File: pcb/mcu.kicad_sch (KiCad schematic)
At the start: 23 parts, among them J1 AVR-ISP-6, U15 TL431DBZ, U6 ATmega328P-AU, Y1 14.7456 MHz

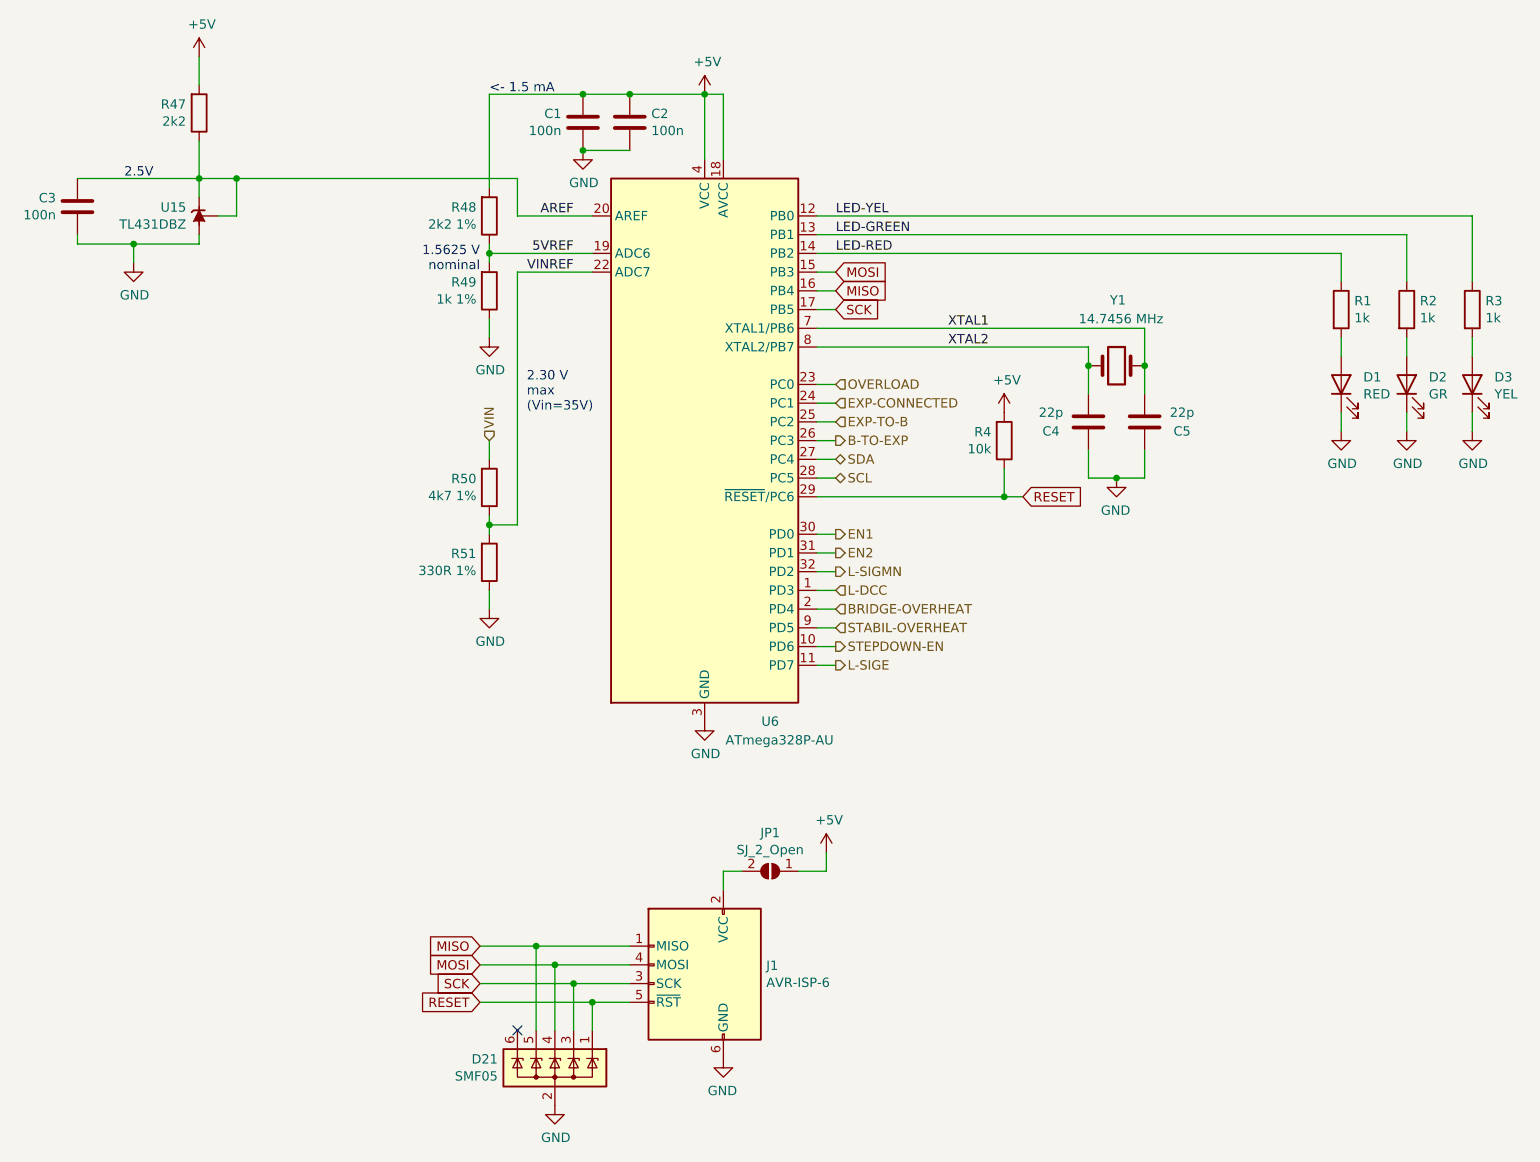
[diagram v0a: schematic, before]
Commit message: Update to KiCad 8.
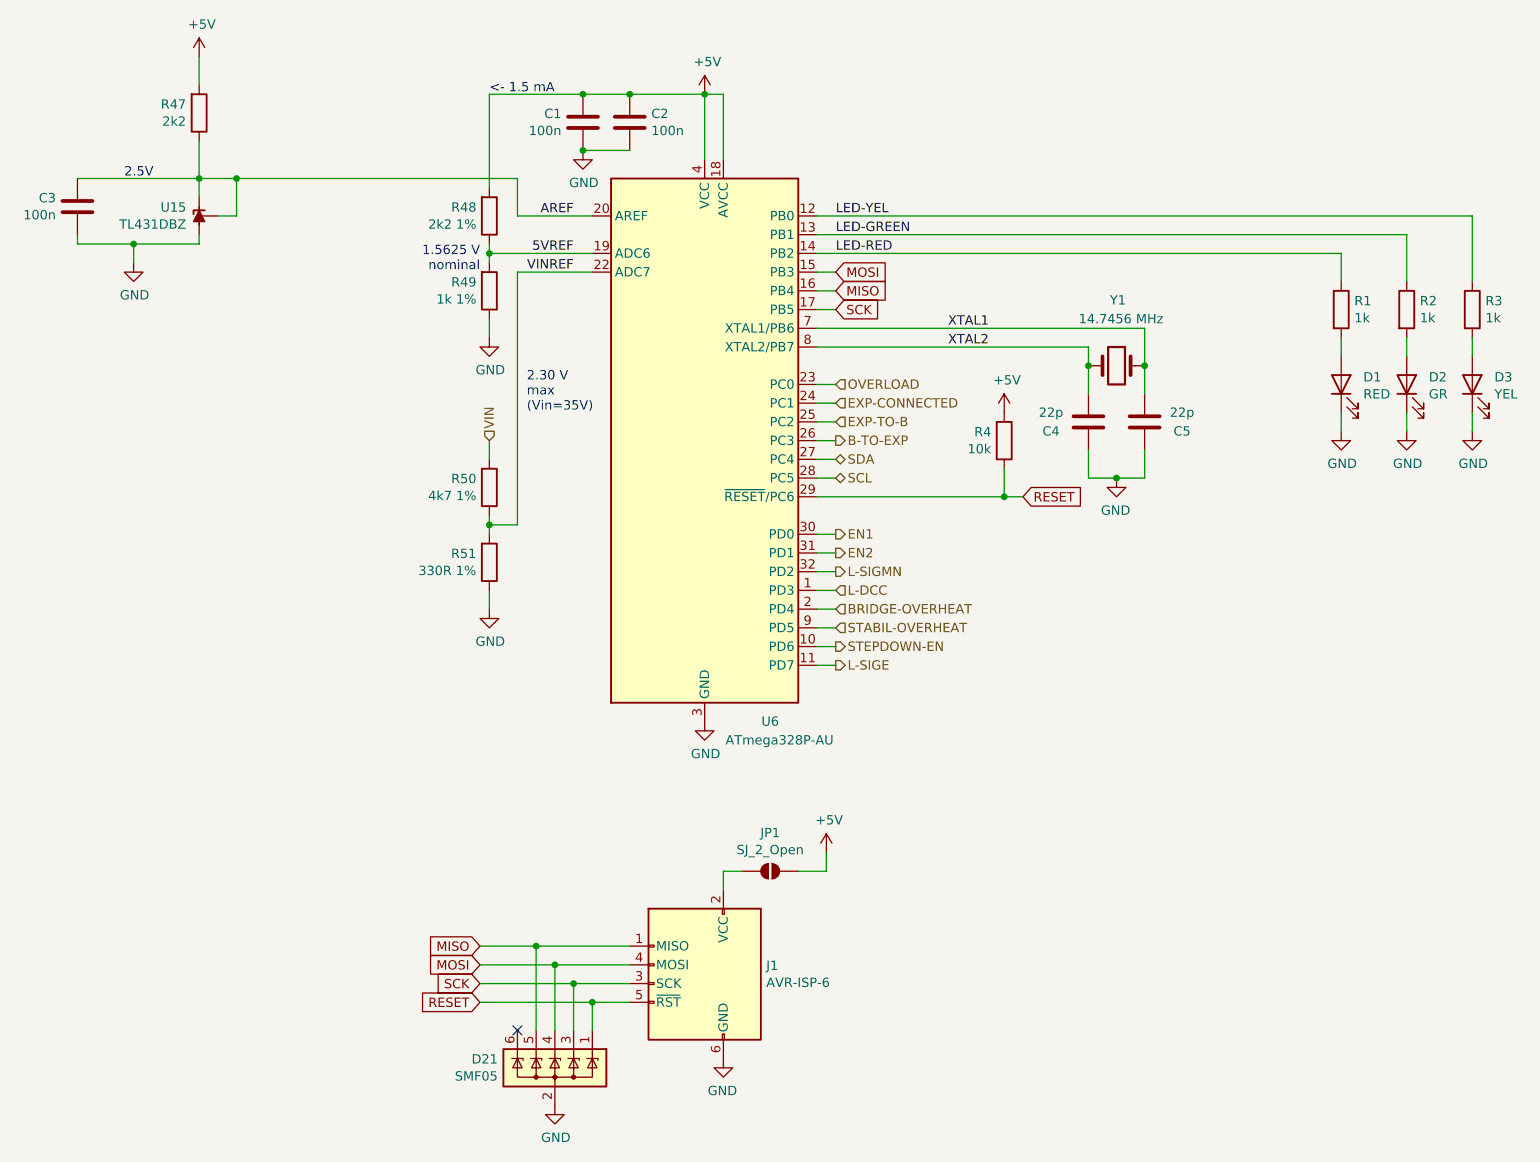
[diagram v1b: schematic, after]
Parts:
- U6: symbol MCU_Microchip_ATmega:ATmega328P-AU -> MCU_Microchip_ATmega:ATmega328P-A

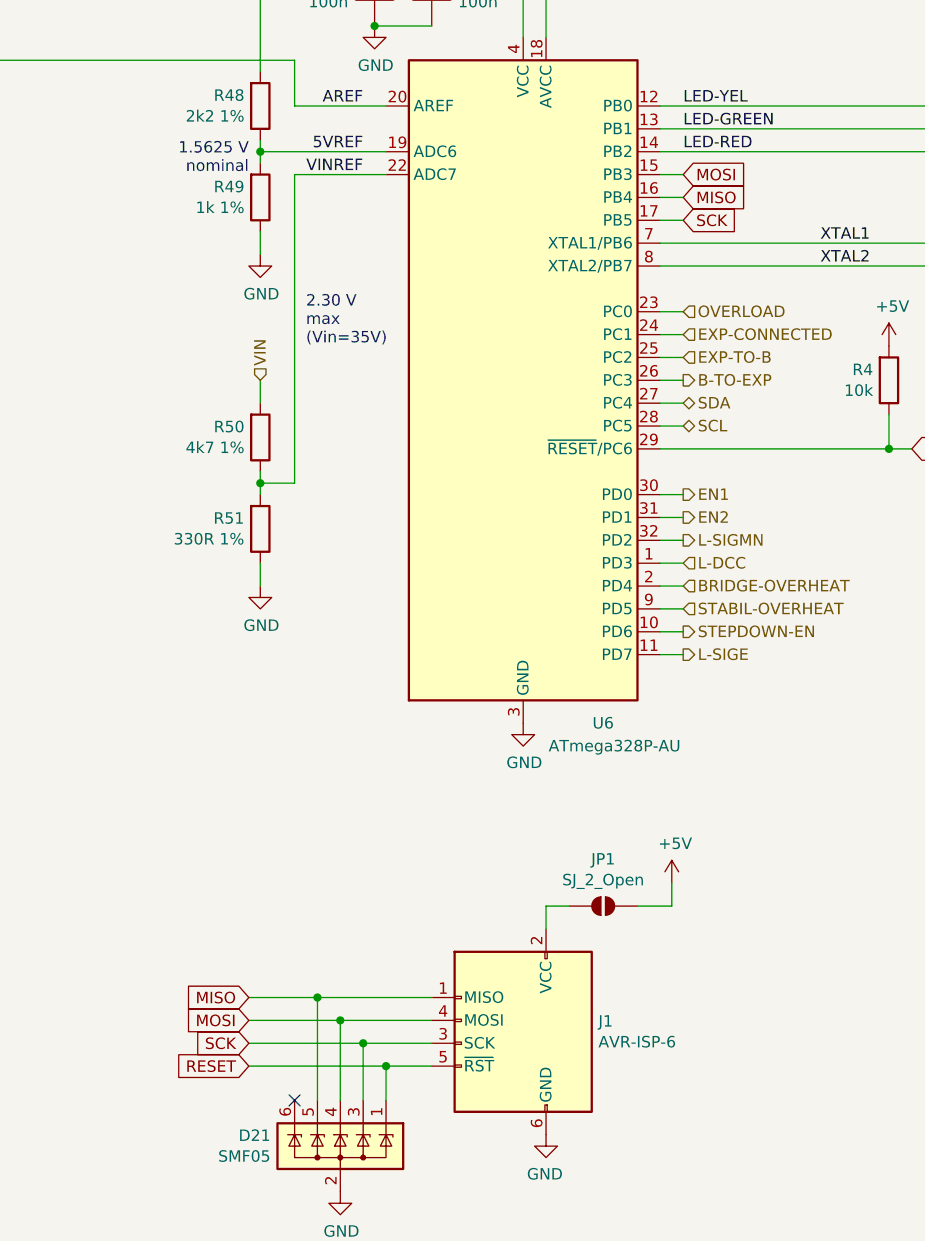
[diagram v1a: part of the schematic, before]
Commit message: Use 1N5819 instead of 1N4148.
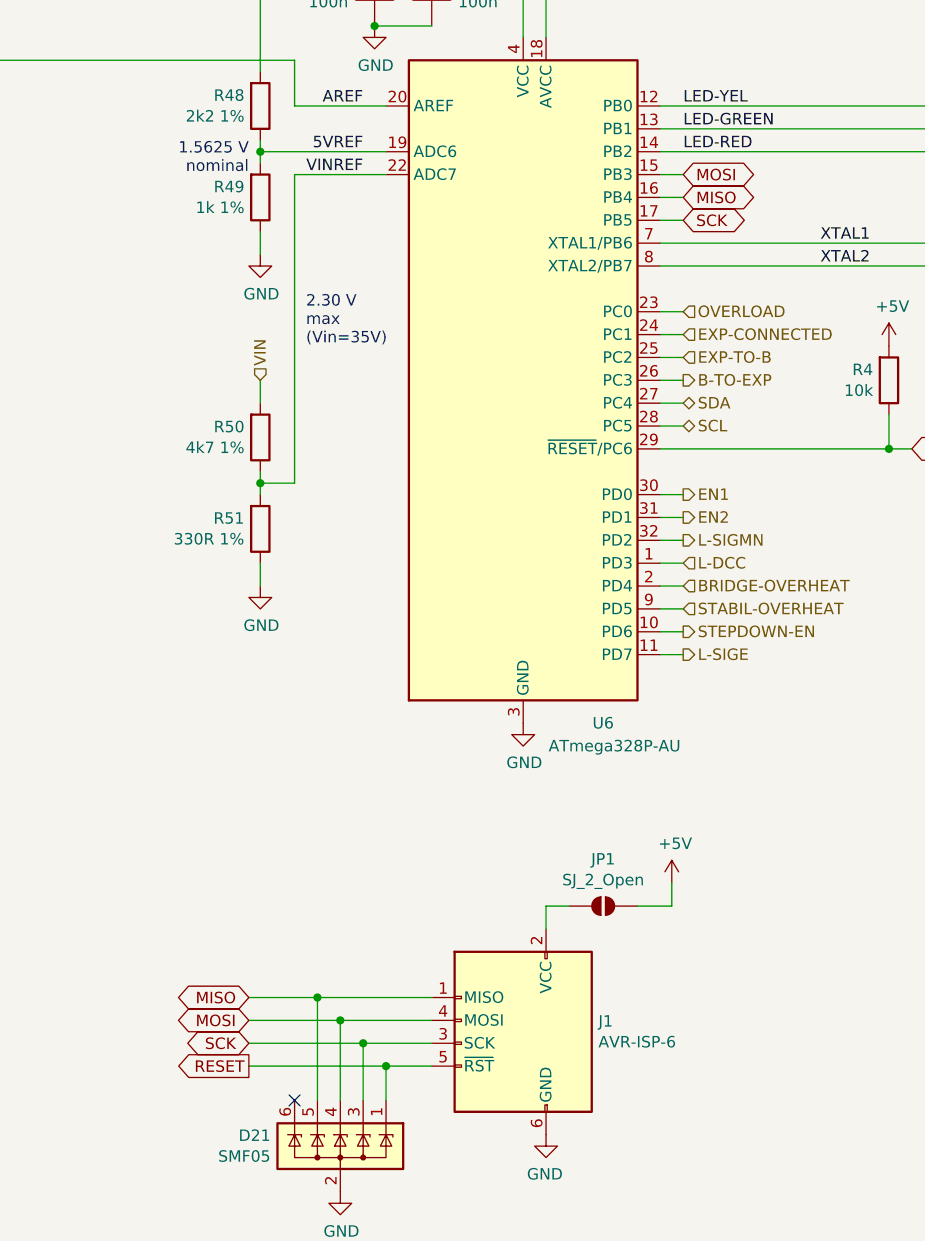
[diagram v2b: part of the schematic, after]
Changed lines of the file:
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@@
 	)
 	(global_label "SCK"
-		(shape input)
+		(shape bidirectional)
 		(at 106.68 154.94 180)
 		(fields_autoplaced yes)
@@
 		)
 		(property "Intersheetrefs" "${INTERSHEET_REFS}"
-			(at 100.5995 154.94 0)
+			(at 99.647 154.94 0)
 			(effects
 				(font
@@
 	)
 	(global_label "SCK"
-		(shape input)
+		(shape bidirectional)
 		(at 154.94 63.5 0)
 		(fields_autoplaced yes)
@@
 		)
 		(property "Intersheetrefs" "${INTERSHEET_REFS}"
-			(at 161.0205 63.5 0)
+			(at 161.973 63.5 0)
 			(effects
 				(font
@@
 	)
 	(global_label "RESET"
-		(shape input)
+		(shape output)
 		(at 106.68 157.48 180)
 		(fields_autoplaced yes)
@@
 	)
 	(global_label "MISO"
-		(shape input)
+		(shape bidirectional)
 		(at 106.68 149.86 180)
 		(fields_autoplaced yes)
@@
 		)
 		(property "Intersheetrefs" "${INTERSHEET_REFS}"
-			(at 99.7528 149.86 0)
+			(at 98.8003 149.86 0)
 			(effects
 				(font
@@
 	)
 	(global_label "MOSI"
-		(shape input)
+		(shape bidirectional)
 		(at 106.68 152.4 180)
 		(fields_autoplaced yes)
@@
 		)
 		(property "Intersheetrefs" "${INTERSHEET_REFS}"
-			(at 99.7528 152.4 0)
+			(at 98.8003 152.4 0)
 			(effects
 				(font
@@
 	)
 	(global_label "MISO"
-		(shape input)
+		(shape bidirectional)
 		(at 154.94 60.96 0)
 		(fields_autoplaced yes)
@@
 		)
 		(property "Intersheetrefs" "${INTERSHEET_REFS}"
-			(at 161.8672 60.96 0)
+			(at 162.8197 60.96 0)
 			(effects
 				(font
@@
 	)
 	(global_label "MOSI"
-		(shape input)
+		(shape bidirectional)
 		(at 154.94 58.42 0)
 		(fields_autoplaced yes)
@@
 		)
 		(property "Intersheetrefs" "${INTERSHEET_REFS}"
-			(at 161.8672 58.42 0)
+			(at 162.8197 58.42 0)
 			(effects
 				(font

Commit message: Export root page escription to other pages.
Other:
- title: HB22 – microcontroller -> HB22 – DCC booster
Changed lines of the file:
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@@
 	(paper "A4")
 	(title_block
-		(title "HB22 – microcontroller")
-		(date "2021-12-28")
+		(title "HB22 – DCC booster")
+		(date "2025-02-20")
 		(rev "1.0")
 		(company "Model Railroader Club Brno I – KMŽ Brno I – https://kmz-brno.cz/")

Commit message: Use normal SMD footprints, avoid handsolder.
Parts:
- C1, C2, C3, C4, C5: footprint Capacitor_SMD:C_0805_2012Metric_Pad1.18x1.45mm_HandSolder -> Capacitor_SMD:C_0805_2012Metric
- D1, D2, D3: footprint LED_SMD:LED_0805_2012Metric_Pad1.15x1.40mm_HandSolder -> LED_SMD:LED_0805_2012Metric
- R1, R2, R3, R4, R47, R48, R49, R50, R51: footprint Resistor_SMD:R_0805_2012Metric_Pad1.20x1.40mm_HandSolder -> Resistor_SMD:R_0805_2012Metric
- Y1: footprint Crystal:Crystal_SMD_HC49-SD_HandSoldering -> Crystal:Crystal_SMD_HC49-SD
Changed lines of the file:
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@@
 			)
 		)
-		(property "Footprint" "Capacitor_SMD:C_0805_2012Metric_Pad1.18x1.45mm_HandSolder"
+		(property "Footprint" "Capacitor_SMD:C_0805_2012Metric"
 			(at 127.9652 41.91 0)
 			(effects
@@
 			)
 		)
-		(property "Footprint" "Capacitor_SMD:C_0805_2012Metric_Pad1.18x1.45mm_HandSolder"
+		(property "Footprint" "Capacitor_SMD:C_0805_2012Metric"
 			(at 121.6152 34.29 0)
 			(effects
@@
 			)
 		)
-		(property "Footprint" "Capacitor_SMD:C_0805_2012Metric_Pad1.18x1.45mm_HandSolder"
+		(property "Footprint" "Capacitor_SMD:C_0805_2012Metric"
 			(at 53.0352 45.72 0)
 			(effects
@@
 			)
 		)
-		(property "Footprint" "Resistor_SMD:R_0805_2012Metric_Pad1.20x1.40mm_HandSolder"
+		(property "Footprint" "Resistor_SMD:R_0805_2012Metric"
 			(at 176.022 81.28 90)
 			(effects
@@
 			)
 		)
-		(property "Footprint" "Crystal:Crystal_SMD_HC49-SD_HandSoldering"
+		(property "Footprint" "Crystal:Crystal_SMD_HC49-SD"
 			(at 193.04 71.12 0)
 			(effects
@@
 			)
 		)
-		(property "Footprint" "Capacitor_SMD:C_0805_2012Metric_Pad1.18x1.45mm_HandSolder"
+		(property "Footprint" "Capacitor_SMD:C_0805_2012Metric"
 			(at 195.8848 82.55 0)
 			(effects
@@
 			)
 		)
-		(property "Footprint" "Capacitor_SMD:C_0805_2012Metric_Pad1.18x1.45mm_HandSolder"
+		(property "Footprint" "Capacitor_SMD:C_0805_2012Metric"
 			(at 190.1952 74.93 0)
 			(effects
@@
 			)
 		)
-		(property "Footprint" "LED_SMD:LED_0805_2012Metric_Pad1.15x1.40mm_HandSolder"
+		(property "Footprint" "LED_SMD:LED_0805_2012Metric"
 			(at 223.52 73.66 0)
 			(effects
@@
 			)
 		)
-		(property "Footprint" "LED_SMD:LED_0805_2012Metric_Pad1.15x1.40mm_HandSolder"
+		(property "Footprint" "LED_SMD:LED_0805_2012Metric"
 			(at 232.41 73.66 0)
 			(effects
@@
 			)
 		)
-		(property "Footprint" "LED_SMD:LED_0805_2012Metric_Pad1.15x1.40mm_HandSolder"
+		(property "Footprint" "LED_SMD:LED_0805_2012Metric"
 			(at 241.3 73.66 0)
 			(effects
@@
 			)
 		)
-		(property "Footprint" "Resistor_SMD:R_0805_2012Metric_Pad1.20x1.40mm_HandSolder"
+		(property "Footprint" "Resistor_SMD:R_0805_2012Metric"
 			(at 221.742 63.5 90)
 			(effects
@@
 			)
 		)
-		(property "Footprint" "Resistor_SMD:R_0805_2012Metric_Pad1.20x1.40mm_HandSolder"
+		(property "Footprint" "Resistor_SMD:R_0805_2012Metric"
 			(at 230.632 63.5 90)
 			(effects
@@
 			)
 		)
-		(property "Footprint" "Resistor_SMD:R_0805_2012Metric_Pad1.20x1.40mm_HandSolder"
+		(property "Footprint" "Resistor_SMD:R_0805_2012Metric"
 			(at 239.522 63.5 90)
 			(effects
@@
 			)
 		)
-		(property "Footprint" "Resistor_SMD:R_0805_2012Metric_Pad1.20x1.40mm_HandSolder"
+		(property "Footprint" "Resistor_SMD:R_0805_2012Metric"
 			(at 66.802 36.83 90)
 			(effects
@@
 			)
 		)
-		(property "Footprint" "Resistor_SMD:R_0805_2012Metric_Pad1.20x1.40mm_HandSolder"
+		(property "Footprint" "Resistor_SMD:R_0805_2012Metric"
 			(at 106.172 50.8 90)
 			(effects
@@
 			)
 		)
-		(property "Footprint" "Resistor_SMD:R_0805_2012Metric_Pad1.20x1.40mm_HandSolder"
+		(property "Footprint" "Resistor_SMD:R_0805_2012Metric"
 			(at 106.172 60.96 90)
 			(effects
@@
 			)
 		)
-		(property "Footprint" "Resistor_SMD:R_0805_2012Metric_Pad1.20x1.40mm_HandSolder"
+		(property "Footprint" "Resistor_SMD:R_0805_2012Metric"
 			(at 106.172 87.63 90)
 			(effects
@@
 			)
 		)
-		(property "Footprint" "Resistor_SMD:R_0805_2012Metric_Pad1.20x1.40mm_HandSolder"
+		(property "Footprint" "Resistor_SMD:R_0805_2012Metric"
 			(at 106.172 97.79 90)
 			(effects
